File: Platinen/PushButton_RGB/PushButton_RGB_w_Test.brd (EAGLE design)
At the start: 100 x 80 mm, 149 parts, among them IC1 4017D, IC2 4011D, IC3 4017D

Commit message: First Version Push Button 16x RGB
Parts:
- LED1: device led:LED3MM -> led:CHIPLED_0805
- moved C1 1.77 mm to (11.9, 39.7)
- moved LED1 0.81 mm to (13.5, 39.8), turned to 0 degrees
- moved D17 0.79 mm to (14.8, 4.45)
- moved D18 0.48 mm to (17.0, 4.45)
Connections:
- net GND: now also LED1.C; no longer LED1.K
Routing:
- net GND: track 288.4 -> 290.0 mm, vias 5 -> 6
- net N$21: track 2.39 -> 1.53 mm
- net N$71: track 39.1 -> 39.9 mm
- net +5V: track 462.1 -> 461.3 mm
- net N$17: track 54.9 -> 54.2 mm
- net N$76: track 10.6 -> 11.2 mm
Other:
- board text added: ">RELEASE_DATE"
- board text added: "Bot"
- board text added: "INPUT"
- board text added: "OUTPUT"
- board text added: "Push Button-RGB w. Test RGB a. Switch"
- board text added: "Push Button-RGB w. Test-RGB a. Switch"
- board text added: "Push Button-RGB w. Test-RGB a. Switch Vers. 1.0 by Hardi und Jürgen (fromue)"
- board text added: "Top"
- board text added: "green"
- board text removed: "+"
- board text removed: "21.11.2022"
- board text removed: "Push Button-RGB w. Test-RGB"
- board text removed: "PushButton-RGB Vers. 1.0"

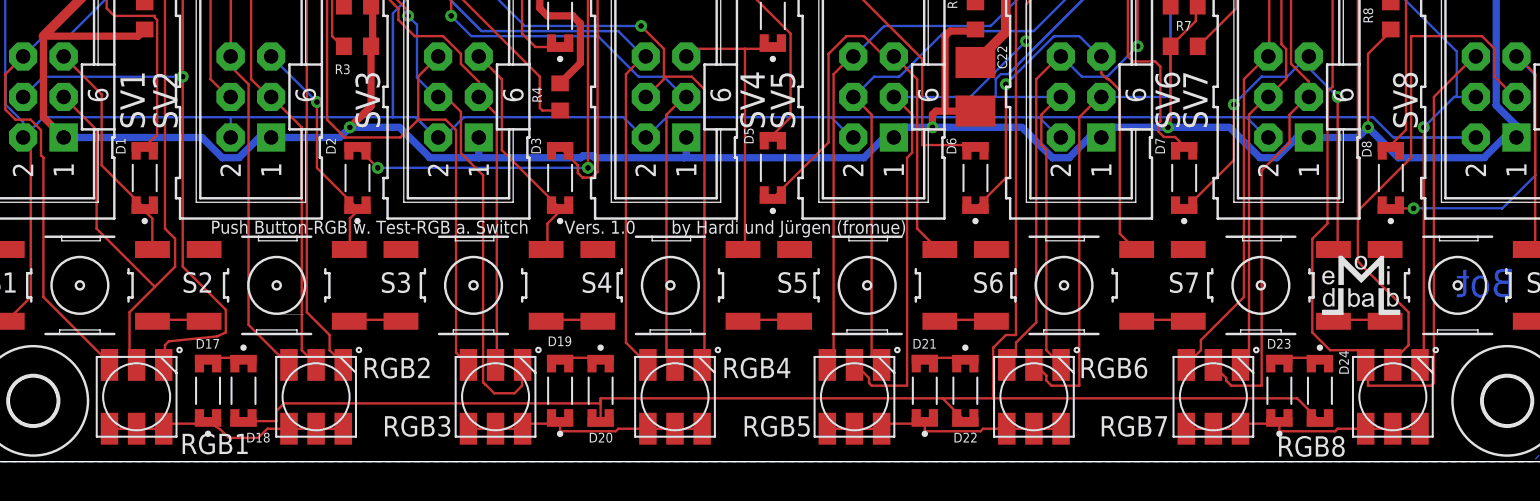
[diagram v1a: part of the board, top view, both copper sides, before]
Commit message: Corrected placement of the diodes at the bottom
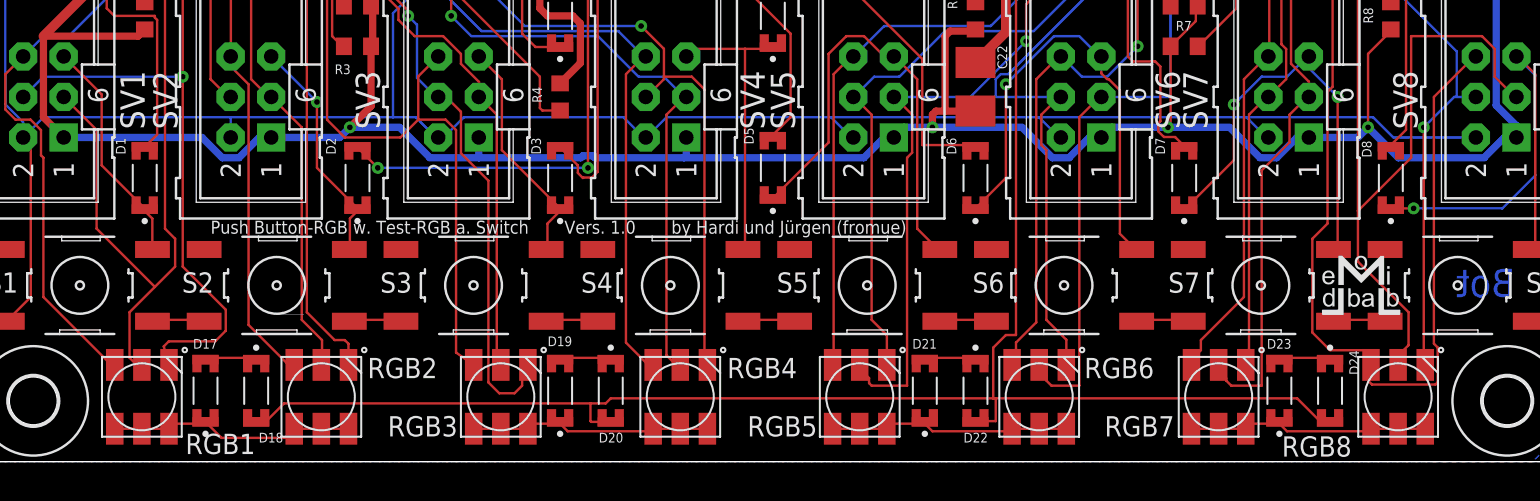
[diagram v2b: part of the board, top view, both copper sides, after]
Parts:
- moved D18 0.79 mm to (17.8, 4.45)
- moved D20 0.64 mm to (40.0, 4.45)
- moved D22 0.64 mm to (62.9, 4.45)
- moved D24 0.64 mm to (85.1, 4.45)
- moved RGB6 0.33 mm to (66.9, 4.06)
- moved RGB1 0.33 mm to (10.6, 4.06)
- moved RGB2 0.33 mm to (21.9, 4.06)
- moved RGB3 0.33 mm to (33.1, 4.06)
- moved RGB4 0.33 mm to (44.4, 4.06)
- moved RGB5 0.33 mm to (55.6, 4.06)
- moved RGB7 0.33 mm to (78.1, 4.06)
- moved RGB8 0.33 mm to (89.4, 4.06)
- moved D17 0.16 mm to (14.6, 4.45)
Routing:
- net N$129: track 15.6 -> 18.5 mm
- net N$20: track 221.3 -> 223.6 mm
- net N$50: track 15.5 -> 17.8 mm
- net N$99: track 15.6 -> 17.8 mm
- net N$72: track 15.6 -> 17.6 mm
- net N$22: track 2.45 -> 3.22 mm
- net N$53: track 2.77 -> 3.40 mm
- net N$43: track 2.77 -> 3.30 mm
- net N$39: track 2.77 -> 3.30 mm
- net N$8: track 42.5 -> 43.0 mm
